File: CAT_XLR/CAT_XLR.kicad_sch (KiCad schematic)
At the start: 9 parts, among them J0 8P8C_Shielded, J1 XLR5, J2 XLR5, J3 XLR5, J4 XLR5, J5 XLR5, J6 XLR5, J7 XLR5, J8 XLR5

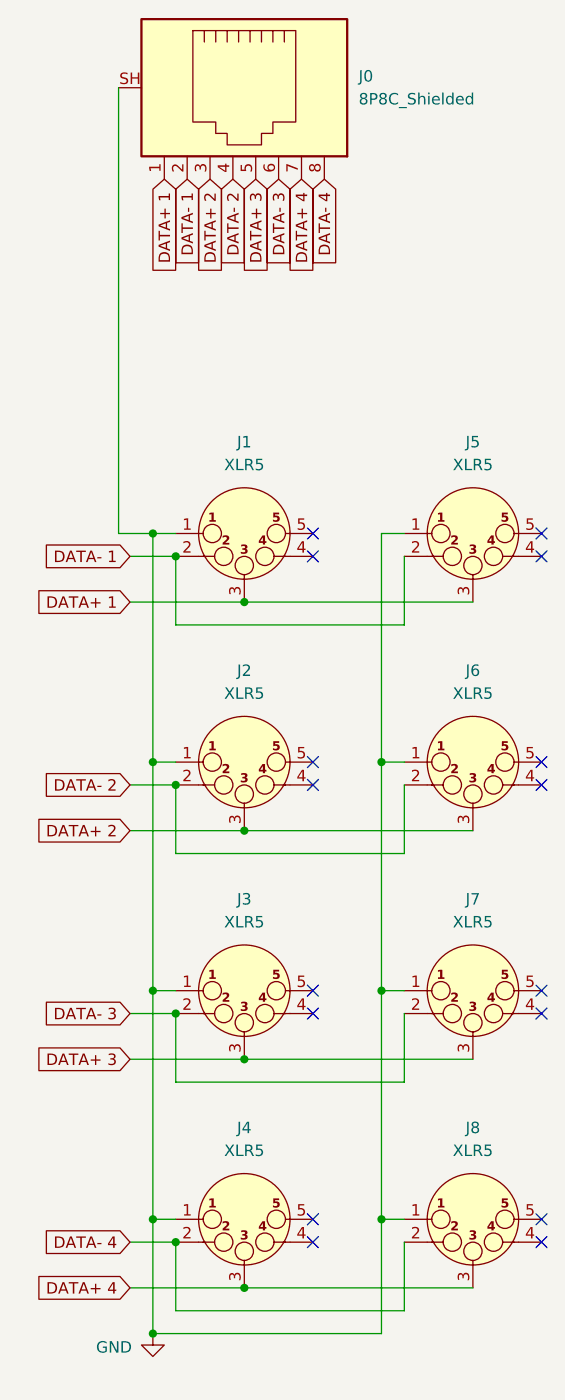
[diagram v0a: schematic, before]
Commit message: fixed CAT connection and gnd connection
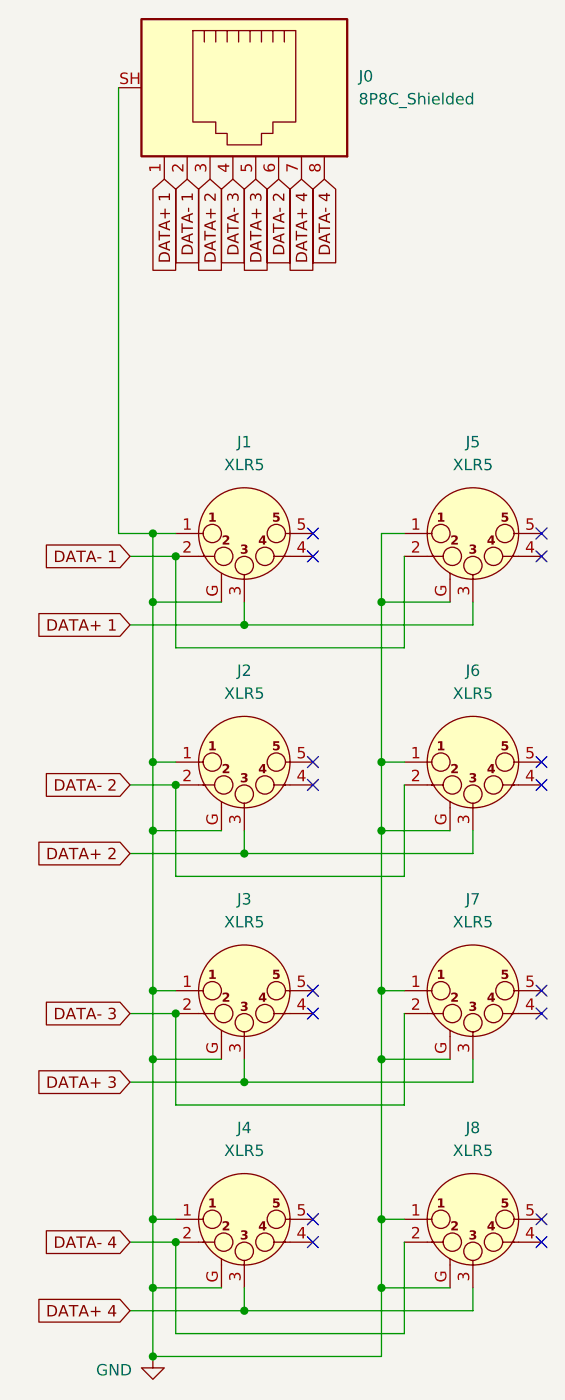
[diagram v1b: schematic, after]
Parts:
- J1, J2, J3, J4, J5, J6, J7, J8: symbol Connector_Audio:XLR5 -> Connector_Audio:XLR5_Ground
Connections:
- net DATA- 2: now also J0.6; no longer J0.4
- net DATA- 3: now also J0.4; no longer J0.6
- net GND: now also J1.G, J2.G, J3.G, J4.G, J5.G, J6.G, J7.G, J8.G
